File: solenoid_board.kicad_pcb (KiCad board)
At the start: 2 copper layers, 90.9 x 93 mm, 38 parts, among them J1 Screw_Terminal_01x02, J10 Screw_Terminal_01x02, J11 Screw_Terminal_01x02, J12 Screw_Terminal_01x06, J13 Conn_01x01_Male, J14 Screw_Terminal_01x06, J2 MCU_LEFT_LEGS, J3 MCU_RIGHT_LEGS, J4 RJ45, J5 RJ45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

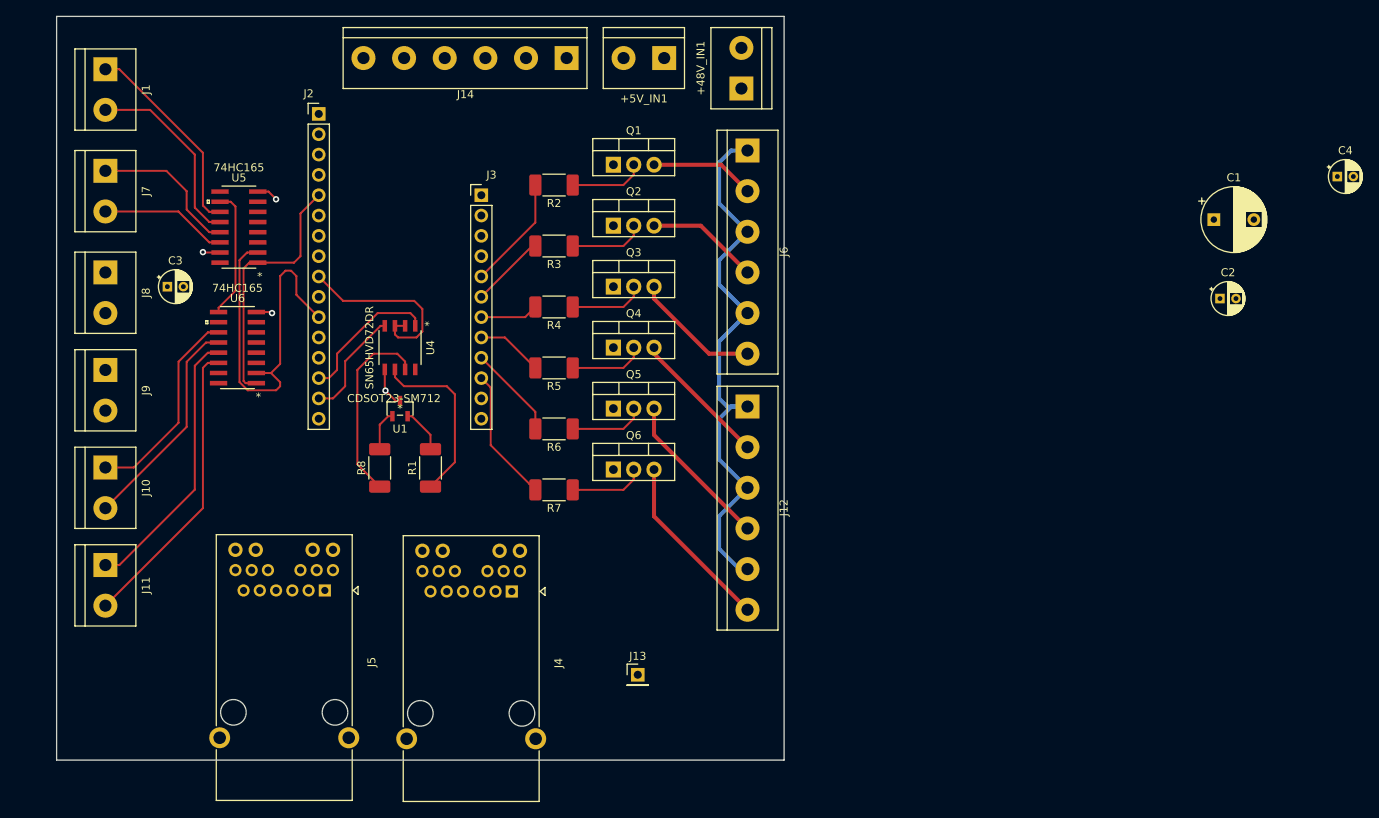
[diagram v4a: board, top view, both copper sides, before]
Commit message: Changed the electrolytic capacitor's footprint, deleted all wires in the layout, and rearranged the components.
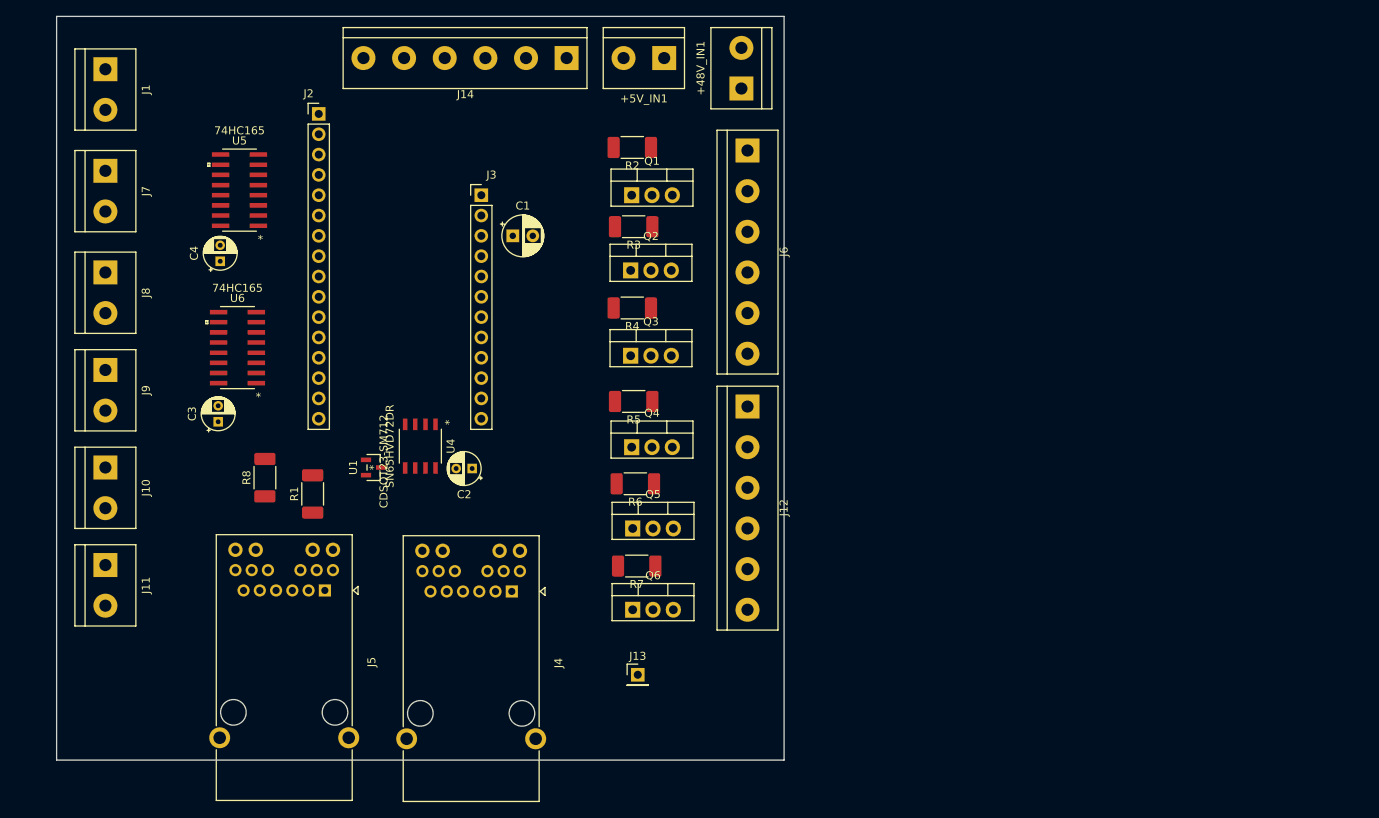
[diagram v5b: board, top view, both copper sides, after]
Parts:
- C1: footprint Capacitor_THT:CP_Radial_D8.0mm_P5.00mm -> Capacitor_THT:CP_Radial_D5.0mm_P2.50mm
- moved C4 140.0 mm to (117.5, 83.9), turned to 90 degrees
- moved C2 95.9 mm to (149.0, 109.9), turned to 180 degrees
- moved C1 87.7 mm to (154.1, 80.8)
- moved C3 18.0 mm to (117.2, 104.0), turned to 90 degrees
- moved Q6 17.7 mm to (169.0, 127.5)
- moved Q5 15.2 mm to (169.0, 117.3)
- moved R1 15.1 mm to (129.0, 113.0)
- moved R8 14.4 mm to (123.1, 111.0)
- moved R7 14.1 mm to (169.5, 122.0)
- moved Q4 12.7 mm to (168.9, 107.2)
- moved U4 12.6 mm to (142.5, 107.1)
- moved R6 12.3 mm to (169.4, 111.8)
- moved R2 10.8 mm to (169.0, 69.7)
- moved R5 10.8 mm to (169.2, 101.5)
- moved R3 10.2 mm to (169.2, 79.6)
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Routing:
- net +48V: track 71.5 -> 0.00 mm
- net /SCK: track 49.1 -> 0.00 mm
- net /INP5_1: track 37.0 -> 0.00 mm
- net /INP5_0: track 34.2 -> 0.00 mm
- net /A0: track 32.1 -> 0.00 mm
- net /INP4_1: track 27.5 -> 0.00 mm
- net /INP4_0: track 25.6 -> 0.00 mm
- net /INP0_0: track 25.6 -> 0.00 mm
- net /INP0_1: track 24.0 -> 0.00 mm
- net /RJ45_5: track 23.9 -> 0.00 mm
- net /A4: track 23.7 -> 0.00 mm
- net Net-(J12-Pad6): track 22.4 -> 0.00 mm
- net /RJ45_4: track 22.2 -> 0.00 mm
- net Net-(J12-Pad4): track 19.8 -> 0.00 mm
- net /INP1_0: track 18.9 -> 0.00 mm
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
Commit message: Increased board size by half a centimeter on the left side so that the 3.3V terminal strip isn't all up in the feather m0's business. Rearranged the PCB layout geometry a bit. Moved the 8-shift registers back to 3.3V because of the volatility of the +5V signal.
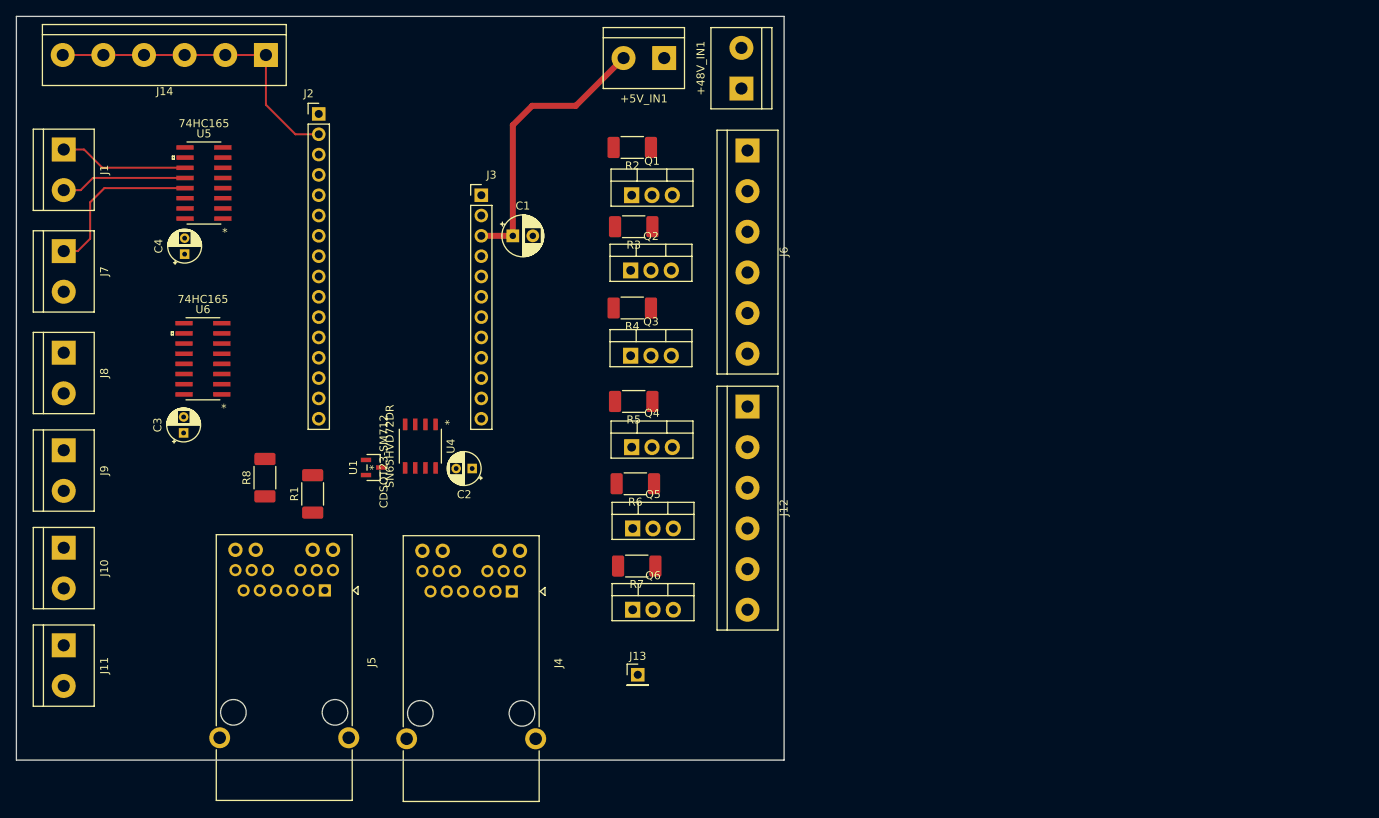
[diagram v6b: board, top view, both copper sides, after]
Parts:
- moved J14 37.6 mm to (123.2, 58.2)
- moved J1 11.3 mm to (97.9, 70.0)
- moved J10 11.3 mm to (97.9, 119.8)
- moved J11 11.3 mm to (97.9, 132.0)
- moved J7 11.3 mm to (97.9, 82.7)
- moved J8 11.3 mm to (97.9, 95.4)
- moved J9 11.3 mm to (97.9, 107.6)
- moved C3 4.54 mm to (112.9, 105.4)
- moved U6 4.54 mm to (115.3, 96.1)
- moved U5 4.53 mm to (115.4, 74.2)
- moved C4 4.53 mm to (113.0, 83.1)
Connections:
- C3 pad 2: +5V -> +3V3
- C4 pad 1: +5V -> +3V3
- U5 pad 16: +5V -> +3V3
- U6 pad 16: +5V -> +3V3
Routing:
- net +3V3: track 0.00 -> 39.8 mm
- net +5V: track 0.00 -> 35.1 mm
- net /INP1_0: track 0.00 -> 21.1 mm
- net /INP0_0: track 0.00 -> 16.1 mm
- net /INP0_1: track 0.00 -> 15.8 mm
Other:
- board size 90.9 x 93 mm -> 96 x 93 mm
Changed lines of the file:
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@@
     (thickness 1.6)
     (drawings 5)
-    (tracks 1)
+    (tracks 29)
     (zones 0)
     (modules 38)
@@
   (setup
     (last_trace_width 0.25)
+    (user_trace_width 0.45)
+    (user_trace_width 0.75)
     (trace_clearance 0.2)
     (zone_clearance 0.508)
@@
   )
   (module TerminalBlock:TerminalBlock_bornier-6_P5.08mm (layer F.Cu)
-    (at 160.782 58.547 180)
+    (at 123.19 58.166 180)
     (descr "simple 6pin terminal block, pitch 5.08mm, revamped version of bornier6")
     (tags "terminal block bornier6")
@@
   )
   (module Capacitor_THT:CP_Radial_D4.0mm_P2.00mm (layer F.Cu)
-    (at 117.475 83.947 90)
+    (at 113.03 83.058 90)
     (descr "CP, Radial series, Radial, pin pitch=2.00mm, , diameter=4mm, Electrolytic Capacitor")
     (tags "CP Radial series Radial pin pitch 2.00mm  diameter 4mm Electrolytic Capacitor")
@@
       (net 13 GND))
     (pad 1 thru_hole rect (at 0 0 90) (size 1.2 1.2) (drill 0.6) (layers *.Cu *.Mask)
-      (net 44 +5V))
+      (net 45 +3V3))
     (model ${KISYS3DMOD}/Capacitor_THT.3dshapes/CP_Radial_D4.0mm_P2.00mm.wrl
       (at (xyz 0 0 0))
@@
   )
   (module Capacitor_THT:CP_Radial_D4.0mm_P2.00mm (layer F.Cu)
-    (at 117.221 104.013 90)
+    (at 112.903 105.41 90)
     (descr "CP, Radial series, Radial, pin pitch=2.00mm, , diameter=4mm, Electrolytic Capacitor")
     (tags "CP Radial series Radial pin pitch 2.00mm  diameter 4mm Electrolytic Capacitor")
@@
     (fp_circle (center 1 0) (end 3 0) (layer F.Fab) (width 0.1))
     (pad 2 thru_hole circle (at 2 0 90) (size 1.2 1.2) (drill 0.6) (layers *.Cu *.Mask)
-      (net 44 +5V))
+      (net 45 +3V3))
     (pad 1 thru_hole rect (at 0 0 90) (size 1.2 1.2) (drill 0.6) (layers *.Cu *.Mask)
       (net 13 GND))
@@
   )
   (module SN74HC165DR:SN74HC165DR (layer F.Cu)
-    (at 119.634 94.742 180)
+    (at 115.316 96.139 180)
     (fp_text reference U6 (at 0 6.171) (layer F.SilkS)
       (effects (font (size 1 1) (thickness 0.15)))
@@
     )
     (pad 16 smd rect (at 2.3622 -4.445 180) (size 2.173199 0.568) (layers F.Cu F.Paste F.Mask)
-      (net 44 +5V))
+      (net 45 +3V3))
     (pad 15 smd rect (at 2.3622 -3.175 180) (size 2.173199 0.568) (layers F.Cu F.Paste F.Mask)
       (net 13 GND))
@@
   )
   (module SN74HC165DR:SN74HC165DR (layer F.Cu)
-    (at 119.888 75.057 180)
+    (at 115.443 74.168 180)
     (fp_text reference U5 (at 0 6.171) (layer F.SilkS)
       (effects (font (size 1 1) (thickness 0.15)))
@@
     )
     (pad 16 smd rect (at 2.3622 -4.445 180) (size 2.173199 0.568) (layers F.Cu F.Paste F.Mask)
-      (net 44 +5V))
+      (net 45 +3V3))
     (pad 15 smd rect (at 2.3622 -3.175 180) (size 2.173199 0.568) (layers F.Cu F.Paste F.Mask)
       (net 13 GND))
@@
   )
   (module TerminalBlock:TerminalBlock_bornier-2_P5.08mm (layer F.Cu)
-    (at 103.124 121.92 270)
+    (at 97.917 131.953 270)
     (descr "simple 2-pin terminal block, pitch 5.08mm, revamped version of bornier2")
     (tags "terminal block bornier2")
@@
   )
   (module TerminalBlock:TerminalBlock_bornier-2_P5.08mm (layer F.Cu)
-    (at 103.124 109.728 270)
+    (at 97.917 119.761 270)
     (descr "simple 2-pin terminal block, pitch 5.08mm, revamped version of bornier2")
     (tags "terminal block bornier2")
@@
   )
   (module TerminalBlock:TerminalBlock_bornier-2_P5.08mm (layer F.Cu)
-    (at 103.124 97.536 270)
+    (at 97.917 107.569 270)
     (descr "simple 2-pin terminal block, pitch 5.08mm, revamped version of bornier2")
     (tags "terminal block bornier2")
@@
   )
   (module TerminalBlock:TerminalBlock_bornier-2_P5.08mm (layer F.Cu)
-    (at 103.124 85.344 270)
+    (at 97.917 95.377 270)
     (descr "simple 2-pin terminal block, pitch 5.08mm, revamped version of bornier2")
     (tags "terminal block bornier2")
@@
   )
   (module TerminalBlock:TerminalBlock_bornier-2_P5.08mm (layer F.Cu)
-    (at 103.124 72.644 270)
+    (at 97.917 82.677 270)
     (descr "simple 2-pin terminal block, pitch 5.08mm, revamped version of bornier2")
     (tags "terminal block bornier2")
@@
   )
   (module TerminalBlock:TerminalBlock_bornier-2_P5.08mm (layer F.Cu)
-    (at 103.124 59.944 270)
+    (at 97.917 69.977 270)
     (descr "simple 2-pin terminal block, pitch 5.08mm, revamped version of bornier2")
     (tags "terminal block bornier2")
@@
   )
   (gr_line (start 187.96 53.34) (end 187.96 146.304) (layer Edge.Cuts) (width 0.1))
-  (gr_line (start 97.028 53.34) (end 187.96 53.34) (layer Edge.Cuts) (width 0.1))
-  (gr_line (start 97.028 146.304) (end 97.028 53.34) (layer Edge.Cuts) (width 0.1))
-  (gr_line (start 187.96 146.304) (end 97.028 146.304) (layer Edge.Cuts) (width 0.1))
+  (gr_line (start 92 53.34) (end 187.96 53.34) (layer Edge.Cuts) (width 0.1))
+  (gr_line (start 92 146.304) (end 92 53.34) (layer Edge.Cuts) (width 0.1))
+  (gr_line (start 187.96 146.304) (end 92 146.304) (layer Edge.Cuts) (width 0.1))
   (dimension 20.32 (width 0.12) (layer F.SilkS)
     (gr_text "0.8000 in" (at 140.208 59.69) (layer F.SilkS)
@@
     (arrow2b (pts (xy 150.368 60.96) (xy 149.241496 61.546421)))
   )
+  (segment (start 99.667 82.677) (end 101.219 81.125) (width 0.25) (layer F.Cu) (net 10))
+  (segment (start 97.917 82.677) (end 99.667 82.677) (width 0.25) (layer F.Cu) (net 10))
+  (segment (start 101.219 81.125) (end 101.219 76.581) (width 0.25) (layer F.Cu) (net 10))
+  (segment (start 102.997 74.803) (end 113.0808 74.803) (width 0.25) (layer F.Cu) (net 10))
+  (segment (start 101.219 76.581) (end 102.997 74.803) (width 0.25) (layer F.Cu) (net 10))
+  (segment (start 100.03832 75.057) (end 101.56232 73.533) (width 0.25) (layer F.Cu) (net 11))
+  (segment (start 97.917 75.057) (end 100.03832 75.057) (width 0.25) (layer F.Cu) (net 11))
+  (segment (start 101.56232 73.533) (end 113.0808 73.533) (width 0.25) (layer F.Cu) (net 11))
+  (segment (start 97.917 69.977) (end 100.457 69.977) (width 0.25) (layer F.Cu) (net 12))
+  (segment (start 102.743 72.263) (end 113.0808 72.263) (width 0.25) (layer F.Cu) (net 12))
+  (segment (start 100.457 69.977) (end 102.743 72.263) (width 0.25) (layer F.Cu) (net 12))
   (segment (start 166.648 88.924) (end 166.648 89.789) (width 0.25) (layer F.Cu) (net 23) (status 30))
+  (segment (start 154.051 80.772) (end 150.114 80.772) (width 0.75) (layer F.Cu) (net 44))
+  (segment (start 154.051 80.772) (end 154.051 66.929) (width 0.75) (layer F.Cu) (net 44))
+  (segment (start 154.051 66.929) (end 156.464 64.516) (width 0.75) (layer F.Cu) (net 44))
+  (segment (start 161.925 64.516) (end 167.894 58.547) (width 0.75) (layer F.Cu) (net 44))
+  (segment (start 156.464 64.516) (end 161.925 64.516) (width 0.75) (layer F.Cu) (net 44))
+  (segment (start 129.794 68.072) (end 126.873 68.072) (width 0.25) (layer F.Cu) (net 45))
+  (segment (start 123.19 64.389) (end 123.19 58.166) (width 0.25) (layer F.Cu) (net 45))
+  (segment (start 126.873 68.072) (end 123.19 64.389) (width 0.25) (layer F.Cu) (net 45))
+  (segment (start 121.44 58.166) (end 118.11 58.166) (width 0.25) (layer F.Cu) (net 45))
+  (segment (start 123.19 58.166) (end 121.44 58.166) (width 0.25) (layer F.Cu) (net 45))
+  (segment (start 115.98868 58.166) (end 113.03 58.166) (width 0.25) (layer F.Cu) (net 45))
+  (segment (start 118.11 58.166) (end 115.98868 58.166) (width 0.25) (layer F.Cu) (net 45))
+  (segment (start 113.03 58.166) (end 107.95 58.166) (width 0.25) (layer F.Cu) (net 45))
+  (segment (start 105.82868 58.166) (end 102.87 58.166) (width 0.25) (layer F.Cu) (net 45))
+  (segment (start 107.95 58.166) (end 105.82868 58.166) (width 0.25) (layer F.Cu) (net 45))
+  (segment (start 100.74868 58.166) (end 97.79 58.166) (width 0.25) (layer F.Cu) (net 45))
+  (segment (start 102.87 58.166) (end 100.74868 58.166) (width 0.25) (layer F.Cu) (net 45))
 )

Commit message: Laid about half the wire. Next Step, lay out the wires for the digital electronics
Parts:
- moved J6 30.5 mm to (182.9, 100.6), turned to 90 degrees
- moved J12 30.5 mm to (183.0, 132.6), turned to 90 degrees
- moved Q3 20.6 mm to (169.0, 75.2)
- moved R4 20.6 mm to (169.2, 69.2)
- moved R7 20.3 mm to (169.3, 101.7)
- moved R5 20.3 mm to (169.3, 121.8)
- moved Q4 20.3 mm to (169.0, 127.5)
- moved Q6 20.3 mm to (169.0, 107.2)
- moved R2 20.2 mm to (169.0, 89.9)
- moved Q1 19.8 mm to (168.8, 95.5)
- moved C4 2.03 mm to (113.0, 81.0), turned to 270 degrees
- moved Q2 0.36 mm to (169.0, 85.3)
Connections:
- R2 pad 2: /D12 -> /D10
- R4 pad 2: /D10 -> /D12
- R5 pad 2: /D9 -> /D5
- R7 pad 2: /D5 -> /D9
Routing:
- net +48V: track 0.00 -> 101.0 mm, vias 0 -> 1
- net /RJ45_5: track 0.00 -> 70.2 mm, vias 0 -> 2
- net /RJ45_4: track 0.00 -> 60.1 mm
- net /D5: track 0.00 -> 30.9 mm
- net /D12: track 0.00 -> 30.0 mm
- net /D6: track 0.00 -> 25.8 mm
- net /D11: track 0.00 -> 20.3 mm
- net /D9: track 0.00 -> 20.3 mm
- net /D10: track 0.86 -> 17.0 mm
- net Net-(R8-Pad2): track 0.00 -> 12.7 mm
- net Net-(J6-Pad2): track 0.00 -> 9.02 mm
- net Net-(J12-Pad6): track 0.00 -> 8.89 mm
- net Net-(J12-Pad4): track 0.00 -> 8.89 mm
- net Net-(J12-Pad2): track 0.00 -> 8.89 mm
- net Net-(J6-Pad6): track 0.00 -> 8.76 mm
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
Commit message: Wired up the RS-485 Transciever
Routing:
- net +3V3: track 47.6 -> 101.1 mm
- net /A4: track 0.00 -> 29.2 mm, vias 0 -> 2
- net /RX0: track 0.00 -> 18.5 mm
- net /TX1: track 0.00 -> 12.7 mm
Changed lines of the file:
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@@
     (thickness 1.6)
     (drawings 5)
-    (tracks 135)
+    (tracks 157)
     (zones 0)
     (modules 38)
@@
     (arrow2b (pts (xy 150.368 60.96) (xy 149.241496 61.546421)))
   )
-  (via (at 179.705 69.85) (size 1.4) (drill 0.7) (layers F.Cu B.Cu) (net 26))
   (segment (start 99.667 82.677) (end 101.219 81.125) (width 0.25) (layer F.Cu) (net 10))
   (segment (start 97.917 82.677) (end 99.667 82.677) (width 0.25) (layer F.Cu) (net 10))
@@
   (segment (start 102.743 72.263) (end 113.0808 72.263) (width 0.25) (layer F.Cu) (net 12))
   (segment (start 100.457 69.977) (end 102.743 72.263) (width 0.25) (layer F.Cu) (net 12))
+  (segment (start 130.996081 101.092) (end 129.794 101.092) (width 0.25) (layer F.Cu) (net 14))
+  (segment (start 138.318797 101.092) (end 130.996081 101.092) (width 0.25) (layer F.Cu) (net 14))
+  (segment (start 140.589 103.362203) (end 138.318797 101.092) (width 0.25) (layer F.Cu) (net 14))
+  (segment (start 140.589 104.339652) (end 140.589 103.362203) (width 0.25) (layer F.Cu) (net 14))
+  (segment (start 141.097 98.552) (end 129.794 98.552) (width 0.25) (layer F.Cu) (net 15))
+  (segment (start 144.399 104.339652) (end 144.399 101.854) (width 0.25) (layer F.Cu) (net 15))
+  (segment (start 144.399 101.854) (end 141.097 98.552) (width 0.25) (layer F.Cu) (net 15))
+  (segment (start 143.129 104.339652) (end 141.859 104.339652) (width 0.25) (layer F.Cu) (net 18))
+  (segment (start 141.859 104.339652) (end 141.859 102.108) (width 0.25) (layer F.Cu) (net 18))
+  (segment (start 141.859 102.108) (end 141.859 102.108) (width 0.25) (layer F.Cu) (net 18))
+  (via (at 141.859 102.108) (size 0.8) (drill 0.4) (layers F.Cu B.Cu) (net 18))
+  (segment (start 141.859 102.108) (end 139.446 99.695) (width 0.25) (layer B.Cu) (net 18))
+  (segment (start 139.446 99.695) (end 139.319 99.568) (width 0.25) (layer B.Cu) (net 18))
+  (segment (start 139.319 99.568) (end 139.319 97.155) (width 0.25) (layer B.Cu) (net 18))
+  (segment (start 139.319 97.155) (end 139.319 97.155) (width 0.25) (layer B.Cu) (net 18))
+  (via (at 139.319 97.155) (size 0.8) (drill 0.4) (layers F.Cu B.Cu) (net 18))
+  (segment (start 137.414 85.852) (end 129.794 85.852) (width 0.25) (layer F.Cu) (net 18))
+  (segment (start 139.319 97.155) (end 139.319 87.757) (width 0.25) (layer F.Cu) (net 18))
+  (segment (start 139.319 87.757) (end 137.414 85.852) (width 0.25) (layer F.Cu) (net 18))
   (segment (start 151.316081 98.552) (end 161.671 108.906919) (width 0.25) (layer F.Cu) (net 20))
   (segment (start 150.114 98.552) (end 151.316081 98.552) (width 0.25) (layer F.Cu) (net 20))
@@
   (segment (start 163.068 69.215) (end 166.902 69.215) (width 0.25) (layer F.Cu) (net 25))
   (segment (start 160.147 72.136) (end 163.068 69.215) (width 0.25) (layer F.Cu) (net 25))
+  (via (at 179.705 69.85) (size 1.4) (drill 0.7) (layers F.Cu B.Cu) (net 26))
   (segment (start 182.626 57.277) (end 179.705 60.198) (width 0.85) (layer F.Cu) (net 26))
   (segment (start 179.705 60.198) (end 179.705 69.723) (width 0.85) (layer F.Cu) (net 26))
@@
   (segment (start 113.03 78.6638) (end 113.0808 78.613) (width 0.25) (layer F.Cu) (net 45))
   (segment (start 113.03 81.026) (end 113.03 78.6638) (width 0.25) (layer F.Cu) (net 45))
+  (segment (start 129.794 68.072) (end 137.668 68.072) (width 0.25) (layer F.Cu) (net 45))
+  (segment (start 146.971 77.375) (end 146.971 109.855) (width 0.25) (layer F.Cu) (net 45))
+  (segment (start 137.668 68.072) (end 146.971 77.375) (width 0.25) (layer F.Cu) (net 45))
 )
